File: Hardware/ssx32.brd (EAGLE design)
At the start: 61 x 60 mm, 74 parts, among them IC1 PIC18LF45K20, IC2 FT232RL, IC3 TXB0108PW, IC4 TXB0108PW, IC5 TXB0108PW, IC6 TXB0108PW, IC7 3V3Regler, X1 8, X10 1, X11 19, X12 16, X13 15, X14 14, X15 13, X16 12, X17 11, X18 10, X19 9, X20 20, X21 21, X22 22, X23 23, X24 24, X25 25, X26 26, X27 27, X28 28, X29 29, X3 17, X30 30, X31 31, X32 32, X33 1751248, X34 18, X35 USB, X4 7, X5 6, X6 5, X7 4, X8 3, X9 2

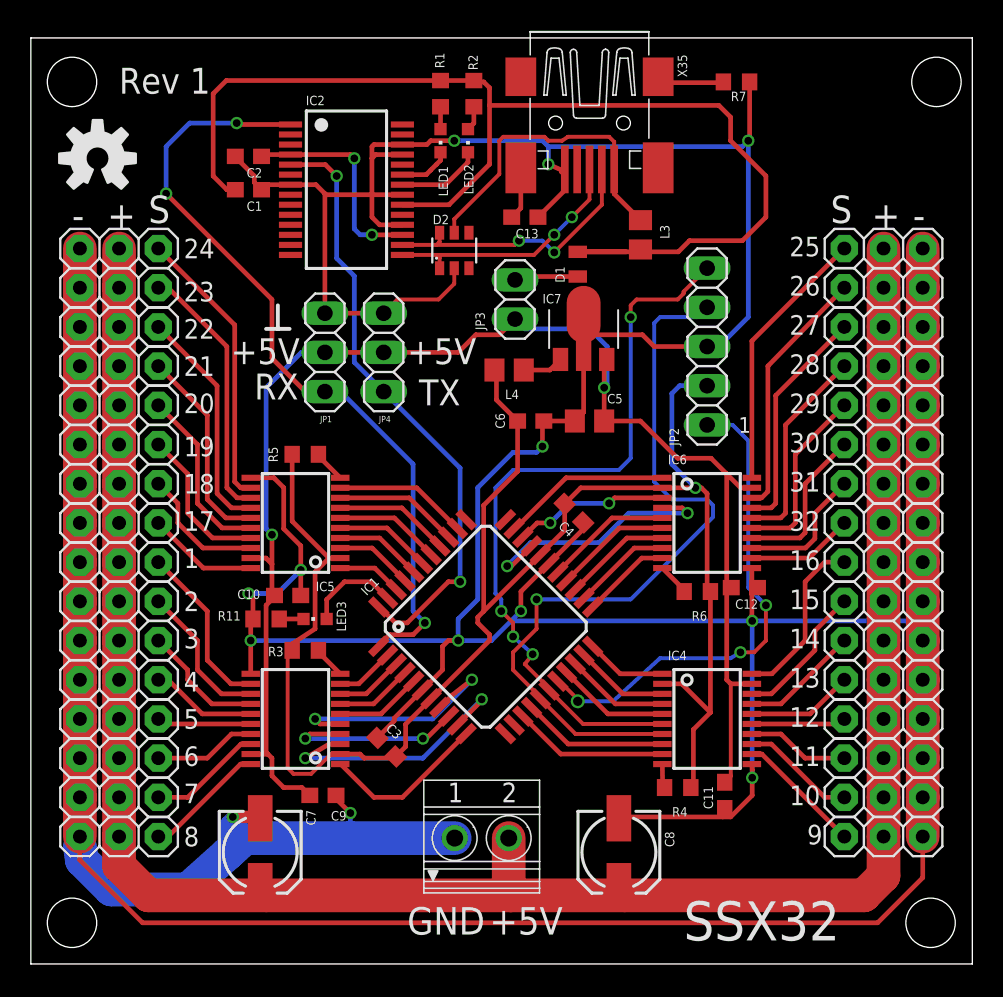
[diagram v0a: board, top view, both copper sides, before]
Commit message: Changed Board
Added polyfuse
Changed component values
Replaced some components for easier PnP
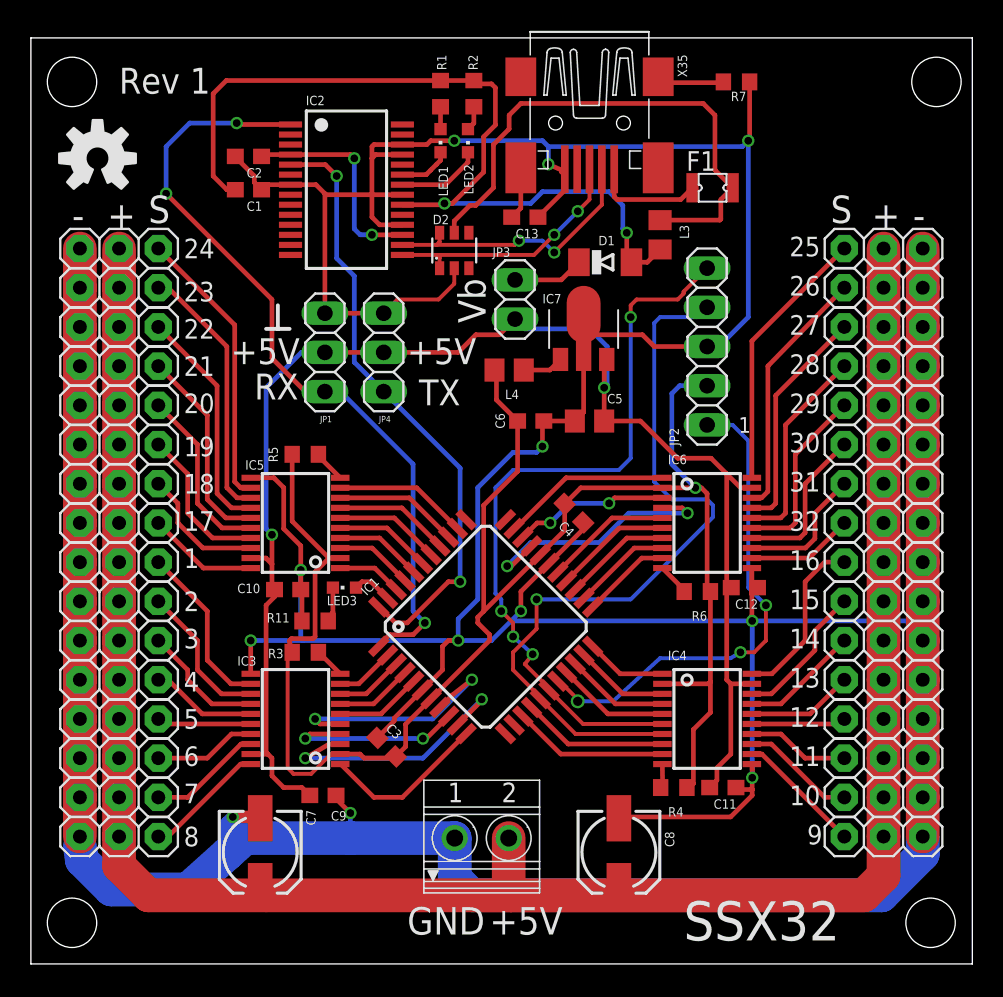
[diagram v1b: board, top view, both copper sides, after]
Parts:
- added F1: NANOSMDC016F, fuse:NANOSMDC016F
- D1: value 0815 -> DO213; device diode:MICROMELF-R -> diode:MINIMELF
- IC7: value 3V3Regler -> 78L33
- moved R11 3.18 mm to (18.4, 22.2)
- moved LED3 2.79 mm to (20.3, 24.4)
- moved D1 1.78 mm to (37.2, 45.5), turned to 0 degrees
- moved L3 1.27 mm to (40.8, 47.2)
- moved C11 0.52 mm to (44.8, 11.4), turned to 180 degrees
- moved C10 0.38 mm to (16.6, 24.3)
- moved R4 0.25 mm to (41.7, 11.4)
- moved R3 0.13 mm to (17.8, 20.2)
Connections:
- new net N$2: F1.1, X35.1
- net N$51: now also F1.2; no longer X35.1
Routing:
- net GND: track 406.4 -> 379.2 mm, vias 13 -> 12
- net +5V: track 77.5 -> 57.0 mm, vias 0 -> 2
- net N$51: track 20.8 -> 34.8 mm
- net N$2: track 0.00 -> 7.24 mm
- net C5: track 6.13 -> 2.64 mm
- net +UB: track 96.2 -> 97.4 mm
- net +3V3: track 112.5 -> 113.2 mm
- net N$45: track 1.57 -> 2.23 mm
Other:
- board text added: "Vb"

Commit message: Error correction
Changed missconnected PIC power supply
Added protection for serial signals
Changed inductors to ferrite beads
Removed voltage select jumper
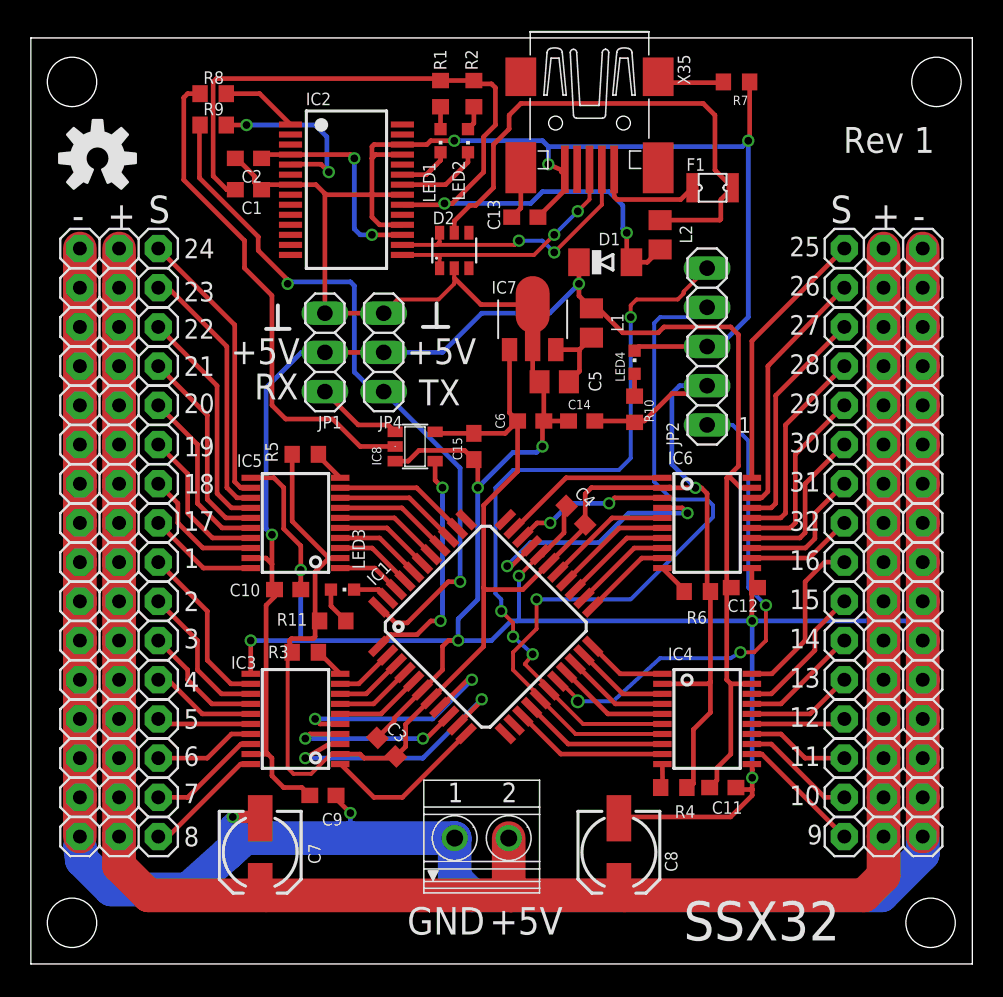
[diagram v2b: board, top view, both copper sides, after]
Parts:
- removed JP3: Vbridge, pinhead:1X02
- removed L4: 10uH, rcl:R0805
- added C14, C15: 100n, rcl:C0603
- added IC8: 74AHC1G32DBV, 74xx-little-de:SOT23-5
- added L1: BLM21PG 300, rcl:R0805
- added LED4: G, led:CHIPLED_0603
- added R10: 330, rcl:R0603
- added R8, R9: 1k, rcl:R0603
- IC1: value PIC18LF45K20 -> PIC18F45K20
- L2: value 10uH -> BLM21PG 300
- R1, R2: value 270 -> 470
- moved C5 3.42 mm to (33.9, 37.7)
- moved IC7 3.36 mm to (32.5, 41.8)
- moved R11 1.14 mm to (19.6, 22.2)
- moved C4 0.18 mm to (35.3, 29.1)
- moved LED3 0.18 mm to (20.2, 24.3), turned to 270 degrees
- moved C2 0.13 mm to (14.1, 52.2)
- renumbered L3 to L2
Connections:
- new net N$52: IC2.5, R9.2
- new net N$53: IC2.1, R8.2
- new net N$54: IC8.1, JP1.1
- new net N$55: LED4.A, R10.1
- net +3V3: now also C14.2, C15.2, C4.1, IC1.28, IC7.1, IC8.5, R10.2, R11.2; no longer C4.2, IC1.29, L4.2
- net +UB: now also D1.C, L1.1; no longer C5.2, IC7.3, JP3.2
- net C5: now also LED3.C; no longer LED3.A
- net GND: now also C14.1, C15.1, C4.2, IC1.29, IC8.3, LED4.C; no longer C4.1, IC1.28, R11.2
- net N$45: now also LED3.A; no longer LED3.C
- net N$46: now also C5.2, IC7.3, L1.2; no longer D1.C, JP3.1
- net N$48: now also IC1.1, IC8.4; no longer IC7.1, L4.1
- net RX: now also IC8.2, R8.1; no longer IC1.1, IC2.1, JP1.1
- net TX: now also R9.1; no longer IC2.5
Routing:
- net RX: track 51.5 -> 32.6 mm, vias 3 -> 0
- net +3V3: track 113.2 -> 128.2 mm
- net N$48: track 3.09 -> 15.3 mm, vias 0 -> 2
- net N$52: track 0.00 -> 11.9 mm, vias 0 -> 2
- net GND: track 379.2 -> 386.9 mm, vias 12 -> 13
- net TX: track 39.7 -> 46.9 mm
- net N$54: track 0.00 -> 5.63 mm
- net +UB: track 97.4 -> 102.6 mm
- net N$53: track 0.00 -> 4.99 mm
- net N$55: track 0.00 -> 1.45 mm
- net +5V: track 57.0 -> 57.5 mm
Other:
- board text removed: "Vb"

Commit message: Added Plane
Added groundplane
Increased servo VCC trace width
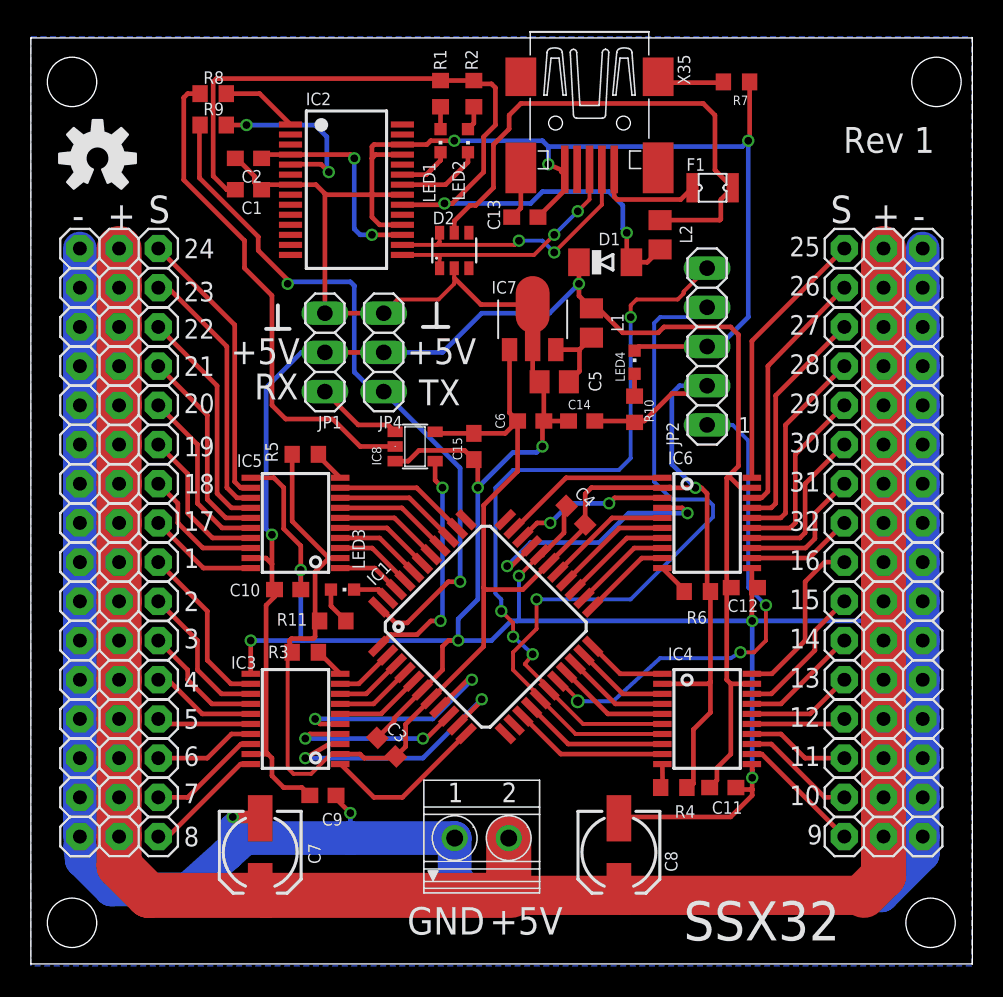
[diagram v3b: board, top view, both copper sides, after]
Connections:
- net N$42 renamed VSERVO
- net N$7 renamed VPORT
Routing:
- added copper zone on layer 16, net GND

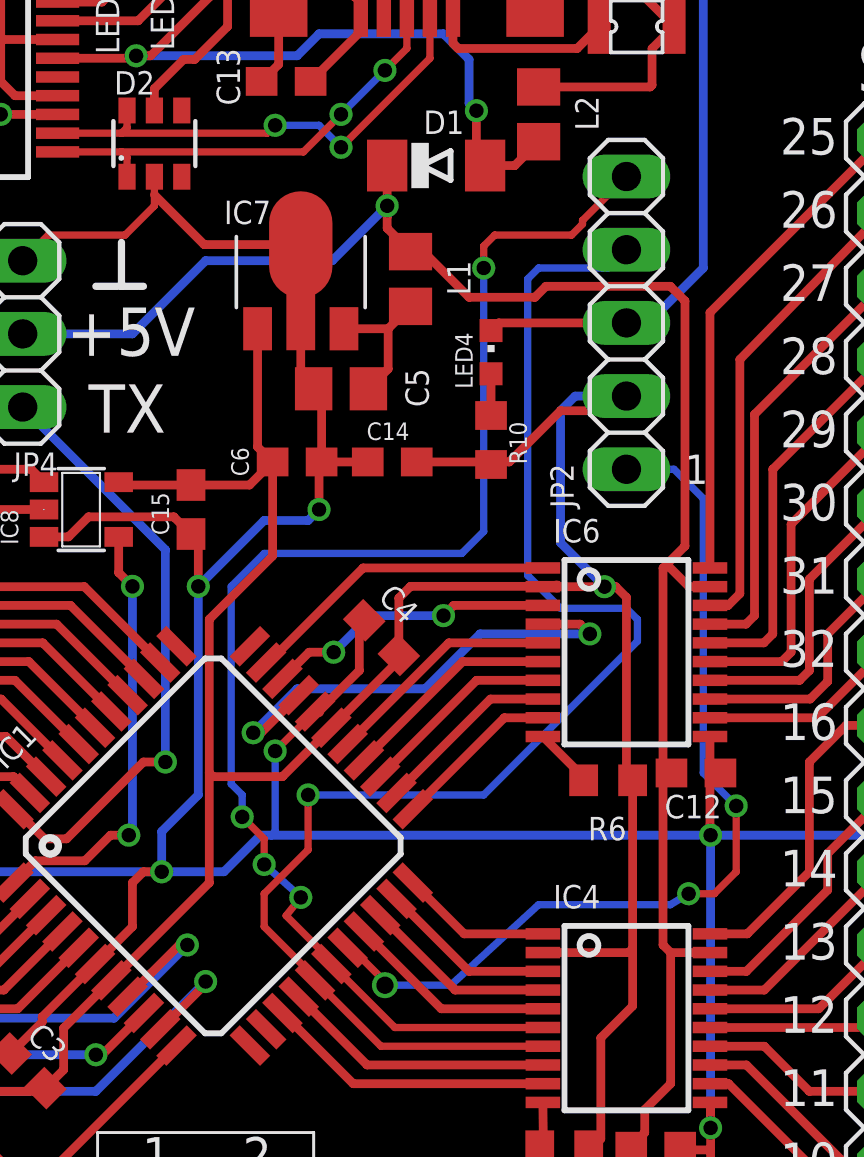
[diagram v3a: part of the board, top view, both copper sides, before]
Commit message: Fixed ICSP interface
Fixed missconnected ICSP interface
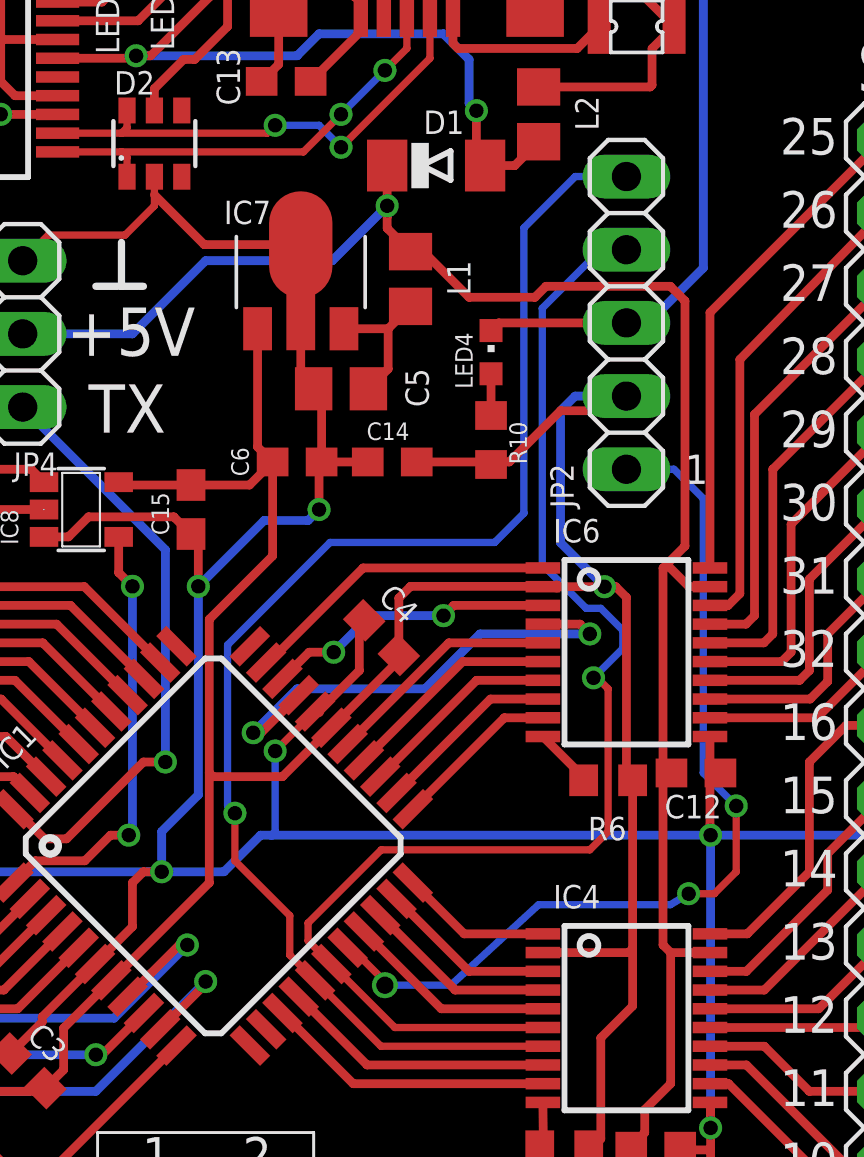
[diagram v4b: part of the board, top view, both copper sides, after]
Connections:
- net B6: now also JP2.5; no longer JP2.4
- net B7: now also JP2.4; no longer JP2.5
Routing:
- net B7: track 48.7 -> 45.8 mm, vias 4 -> 1
- net B6: track 49.6 -> 48.1 mm
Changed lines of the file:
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@@
 <contactref element="IC1" pad="16"/>
 <contactref element="IC4" pad="7"/>
-<contactref element="JP2" pad="4"/>
 <wire x1="35.2945" y1="14.9" x2="40.915" y2="14.9" width="0.254" layer="1"/>
 <wire x1="33.00853125" y1="17.18609375" x2="35.2945" y2="14.9" width="0.254" layer="1"/>
-<wire x1="33.00853125" y1="17.18609375" x2="33.0085" y2="17.2835" width="0.254" layer="1"/>
-<wire x1="33.0085" y1="17.2835" x2="31.242" y2="19.05" width="0.254" layer="1"/>
-<wire x1="31.242" y1="19.05" x2="31.242" y2="20.193" width="0.254" layer="1"/>
-<wire x1="31.242" y1="20.193" x2="32.766" y2="21.717" width="0.254" layer="1"/>
-<wire x1="32.766" y1="21.717" x2="32.766" y2="23.622" width="0.254" layer="1"/>
-<wire x1="32.766" y1="23.622" x2="38.862" y2="23.622" width="0.254" layer="16"/>
-<wire x1="38.862" y1="23.622" x2="44.196" y2="28.956" width="0.254" layer="16"/>
-<wire x1="44.196" y1="28.956" x2="44.196" y2="29.718" width="0.254" layer="16"/>
-<wire x1="44.196" y1="29.718" x2="43.815" y2="30.099" width="0.254" layer="16"/>
-<wire x1="43.815" y1="30.099" x2="41.529" y2="30.099" width="0.254" layer="16"/>
-<wire x1="41.529" y1="30.099" x2="40.386" y2="31.242" width="0.254" layer="16"/>
-<wire x1="40.386" y1="31.242" x2="40.386" y2="41.529" width="0.254" layer="16"/>
-<wire x1="40.386" y1="41.529" x2="40.767" y2="41.91" width="0.254" layer="16"/>
-<wire x1="40.767" y1="41.91" x2="43.18" y2="41.91" width="0.254" layer="16"/>
-<wire x1="43.18" y1="41.91" x2="43.815" y2="42.545" width="0.254" layer="16"/>
-<via x="32.766" y="23.622" extent="1-16" drill="0.5" shape="octagon"/>
+<contactref element="JP2" pad="5"/>
+<wire x1="33.00853125" y1="17.18609375" x2="32.131" y2="18.063625" width="0.254" layer="1"/>
+<wire x1="32.131" y1="18.063625" x2="32.131" y2="19.431" width="0.254" layer="1"/>
+<wire x1="32.131" y1="19.431" x2="30.226" y2="21.336" width="0.254" layer="1"/>
+<wire x1="30.226" y1="21.336" x2="30.226" y2="22.987" width="0.254" layer="1"/>
+<via x="30.226" y="22.987" extent="1-16" drill="0.5" shape="octagon"/>
+<wire x1="30.226" y1="22.987" x2="29.972" y2="23.241" width="0.254" layer="16"/>
+<wire x1="29.972" y1="23.241" x2="29.972" y2="28.829" width="0.254" layer="16"/>
+<wire x1="29.972" y1="28.829" x2="33.528" y2="32.385" width="0.254" layer="16"/>
+<wire x1="33.528" y1="32.385" x2="39.243" y2="32.385" width="0.254" layer="16"/>
+<wire x1="39.243" y1="32.385" x2="40.259" y2="33.401" width="0.254" layer="16"/>
+<wire x1="40.259" y1="33.401" x2="40.259" y2="43.307" width="0.254" layer="16"/>
+<wire x1="40.259" y1="43.307" x2="42.037" y2="45.085" width="0.254" layer="16"/>
+<wire x1="42.037" y1="45.085" x2="43.815" y2="45.085" width="0.254" layer="16"/>
 </signal>
 <signal name="B7">
 <contactref element="IC1" pad="17"/>
 <contactref element="IC4" pad="6"/>
-<contactref element="JP2" pad="5"/>
 <wire x1="35.7759" y1="15.55" x2="40.915" y2="15.55" width="0.254" layer="1"/>
 <wire x1="33.57421875" y1="17.751778125" x2="35.7759" y2="15.55" width="0.254" layer="1"/>
-<wire x1="33.57421875" y1="17.751778125" x2="33.5742" y2="17.8608" width="0.254" layer="1"/>
-<wire x1="33.5742" y1="17.8608" x2="32.004" y2="19.431" width="0.254" layer="1"/>
-<wire x1="32.004" y1="19.431" x2="32.512" y2="20.066" width="0.254" layer="1"/>
-<wire x1="42.291" y1="43.561" x2="43.815" y2="45.085" width="0.254" layer="1"/>
-<wire x1="42.291" y1="43.434" x2="42.291" y2="43.561" width="0.254" layer="1"/>
-<wire x1="41.91" y1="43.053" x2="42.291" y2="43.434" width="0.254" layer="1"/>
-<wire x1="39.243" y1="43.053" x2="41.91" y2="43.053" width="0.254" layer="1"/>
-<wire x1="38.862" y1="42.672" x2="39.243" y2="43.053" width="0.254" layer="1"/>
-<wire x1="38.862" y1="41.91" x2="38.862" y2="42.672" width="0.254" layer="1"/>
-<wire x1="38.862" y1="32.766" x2="38.862" y2="41.91" width="0.254" layer="16"/>
-<wire x1="38.1" y1="32.004" x2="38.862" y2="32.766" width="0.254" layer="16"/>
-<wire x1="31.242" y1="32.004" x2="38.1" y2="32.004" width="0.254" layer="16"/>
-<wire x1="30.099" y1="30.861" x2="31.242" y2="32.004" width="0.254" layer="16"/>
-<wire x1="30.099" y1="24.003" x2="30.099" y2="30.861" width="0.254" layer="16"/>
-<wire x1="30.48" y1="23.622" x2="30.099" y2="24.003" width="0.254" layer="16"/>
-<wire x1="30.48" y1="22.86" x2="30.48" y2="23.622" width="0.254" layer="16"/>
-<wire x1="31.242" y1="22.098" x2="30.48" y2="22.86" width="0.254" layer="1"/>
-<wire x1="31.242" y1="21.209" x2="31.242" y2="22.098" width="0.254" layer="1"/>
-<wire x1="32.385" y1="20.193" x2="31.242" y2="21.209" width="0.254" layer="16"/>
-<wire x1="32.512" y1="20.066" x2="32.385" y2="20.193" width="0.254" layer="16"/>
-<via x="38.862" y="41.91" extent="1-16" drill="0.5" shape="octagon"/>
-<via x="30.48" y="22.86" extent="1-16" drill="0.5" shape="octagon"/>
-<via x="31.242" y="21.209" extent="1-16" drill="0.5" shape="octagon"/>
-<via x="32.512" y="20.066" extent="1-16" drill="0.5" shape="octagon"/>
+<contactref element="JP2" pad="4"/>
+<wire x1="33.57421875" y1="17.751778125" x2="32.766" y2="18.559996875" width="0.254" layer="1"/>
+<wire x1="32.766" y1="18.559996875" x2="32.766" y2="19.177" width="0.254" layer="1"/>
+<wire x1="32.766" y1="19.177" x2="35.306" y2="21.717" width="0.254" layer="1"/>
+<wire x1="35.306" y1="21.717" x2="42.545" y2="21.717" width="0.254" layer="1"/>
+<wire x1="42.545" y1="21.717" x2="43.18" y2="22.352" width="0.254" layer="1"/>
+<wire x1="43.18" y1="22.352" x2="43.18" y2="27.305" width="0.254" layer="1"/>
+<wire x1="43.18" y1="27.305" x2="42.799" y2="27.686" width="0.254" layer="1"/>
+<wire x1="42.799" y1="27.686" x2="42.672" y2="27.686" width="0.254" layer="1"/>
+<via x="42.672" y="27.686" extent="1-16" drill="0.5" shape="octagon"/>
+<wire x1="42.672" y1="27.686" x2="43.688" y2="28.702" width="0.254" layer="16"/>
+<wire x1="43.688" y1="28.702" x2="43.688" y2="29.337" width="0.254" layer="16"/>
+<wire x1="43.688" y1="29.337" x2="42.926" y2="30.099" width="0.254" layer="16"/>
+<wire x1="42.926" y1="30.099" x2="42.418" y2="30.099" width="0.254" layer="16"/>
+<wire x1="42.418" y1="30.099" x2="40.894" y2="31.623" width="0.254" layer="16"/>
+<wire x1="40.894" y1="31.623" x2="40.894" y2="40.513" width="0.254" layer="16"/>
+<wire x1="40.894" y1="40.513" x2="42.926" y2="42.545" width="0.254" layer="16"/>
+<wire x1="42.926" y1="42.545" x2="43.815" y2="42.545" width="0.254" layer="16"/>
 </signal>
 <signal name="N$8">
